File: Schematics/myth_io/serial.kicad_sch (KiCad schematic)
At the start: 7 parts, among them U1 74HC14, U2 74LS02, U5 74AHC04, U6 74HC74, U7 74HC595, U8 74HC165

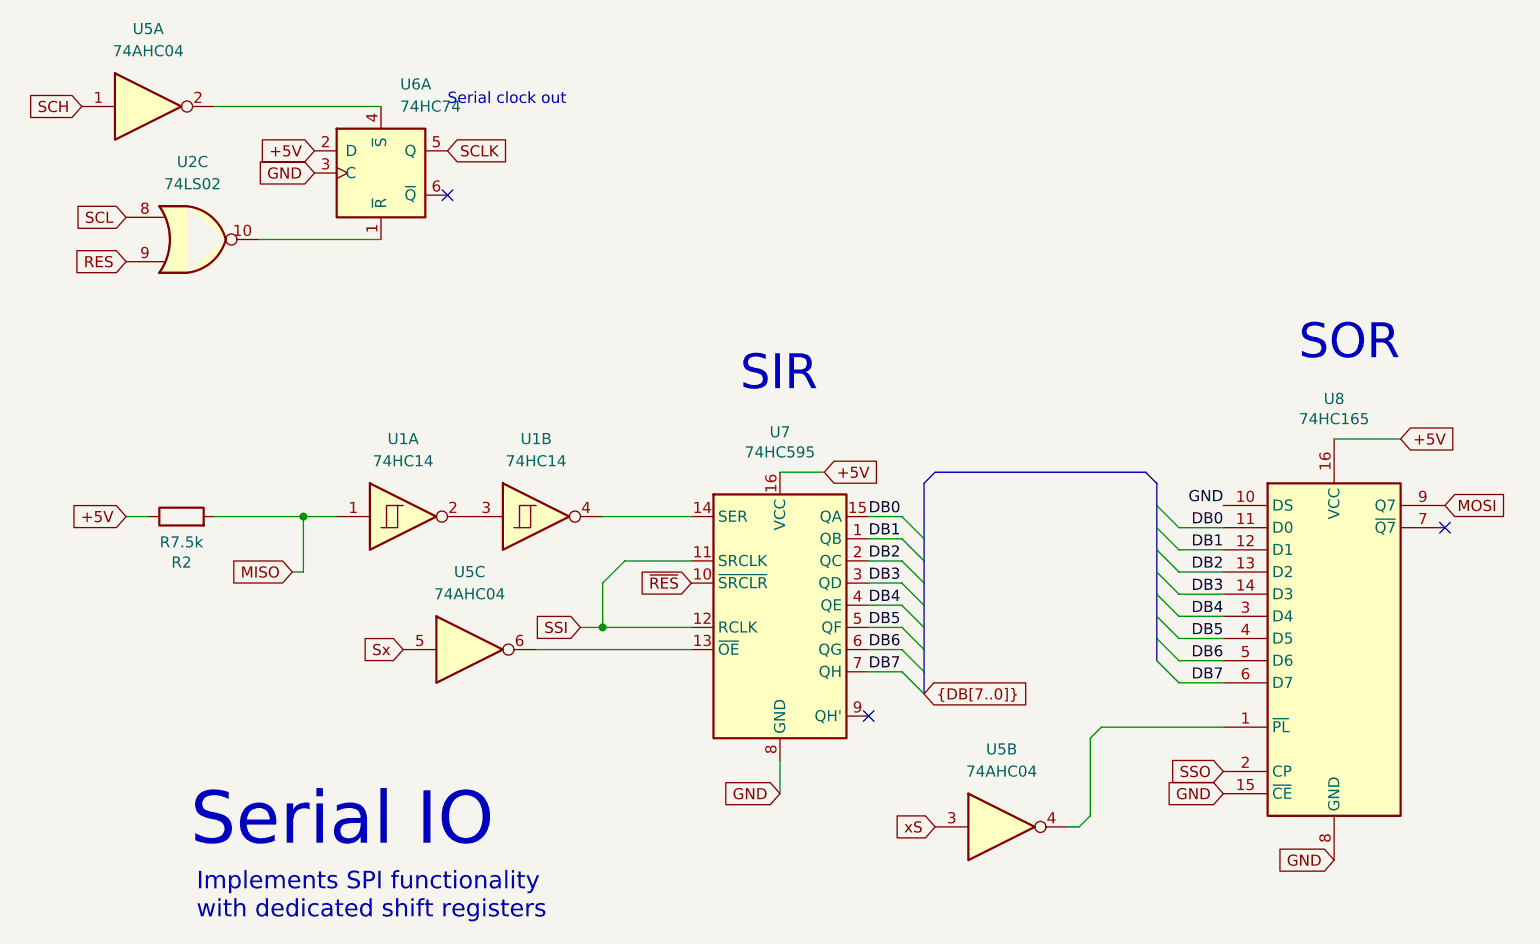
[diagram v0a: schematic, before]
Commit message: Change CO do D
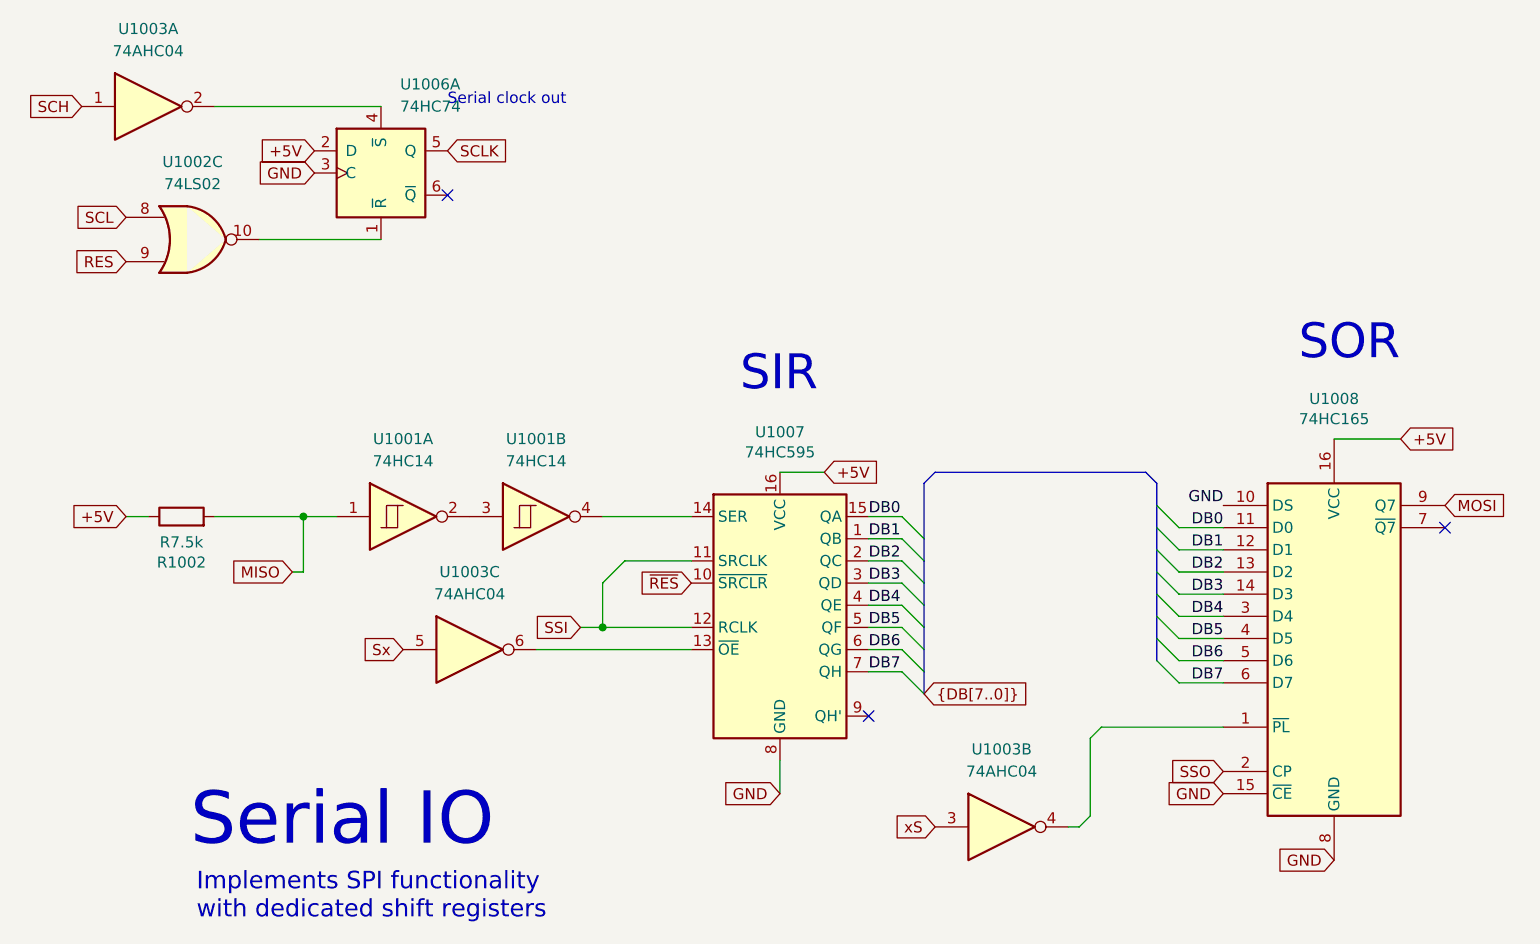
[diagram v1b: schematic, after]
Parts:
- renumbered R2 to R1002, U1 to U1001, U2 to U1002, U5 to U1003, U6 to U1006, U7 to U1007, U8 to U1008
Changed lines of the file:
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@@
 		(dnp no)
 		(fields_autoplaced yes)
-		(property "Reference" "U5"
+		(property "Reference" "U1003"
 			(at 77.47 38.1 0)
 			(effects
@@
 			(project "myth_io"
 				(path "/a907dd88-e0e4-4e6e-a291-053f6213a316/1a18eb1f-a528-4c0e-842f-5264d74e97c6"
-					(reference "U5")
+					(reference "U1003")
 					(unit 1)
 				)
@@
 		(on_board yes)
 		(dnp no)
-		(property "Reference" "U7"
+		(property "Reference" "U1007"
 			(at 149.86 84.3026 0)
 			(effects
@@
 			(project "myth_io"
 				(path "/a907dd88-e0e4-4e6e-a291-053f6213a316/1a18eb1f-a528-4c0e-842f-5264d74e97c6"
-					(reference "U7")
+					(reference "U1007")
 					(unit 1)
 				)
@@
 		(dnp no)
 		(fields_autoplaced yes)
-		(property "Reference" "U5"
+		(property "Reference" "U1003"
 			(at 114.3 100.33 0)
 			(effects
@@
 			(project "myth_io"
 				(path "/a907dd88-e0e4-4e6e-a291-053f6213a316/1a18eb1f-a528-4c0e-842f-5264d74e97c6"
-					(reference "U5")
+					(reference "U1003")
 					(unit 3)
 				)
@@
 		(on_board yes)
 		(dnp no)
-		(property "Reference" "R2"
+		(property "Reference" "R1002"
 			(at 81.28 99.2378 90)
 			(effects
@@
 			(project "myth_io"
 				(path "/a907dd88-e0e4-4e6e-a291-053f6213a316/1a18eb1f-a528-4c0e-842f-5264d74e97c6"
-					(reference "R2")
+					(reference "R1002")
 					(unit 1)
 				)
@@
 		(dnp no)
 		(fields_autoplaced yes)
-		(property "Reference" "U1"
+		(property "Reference" "U1001"
 			(at 106.68 85.09 0)
 			(effects
@@
 			(project "myth_io"
 				(path "/a907dd88-e0e4-4e6e-a291-053f6213a316/1a18eb1f-a528-4c0e-842f-5264d74e97c6"
-					(reference "U1")
+					(reference "U1001")
 					(unit 1)
 				)
@@
 		(on_board yes)
 		(dnp no)
-		(property "Reference" "U8"
+		(property "Reference" "U1008"
 			(at 213.36 80.4926 0)
 			(effects
@@
 			(project "myth_io"
 				(path "/a907dd88-e0e4-4e6e-a291-053f6213a316/1a18eb1f-a528-4c0e-842f-5264d74e97c6"
-					(reference "U8")
+					(reference "U1008")
 					(unit 1)
 				)
@@
 		(dnp no)
 		(fields_autoplaced yes)
-		(property "Reference" "U2"
+		(property "Reference" "U1002"
 			(at 82.55 53.34 0)
 			(effects
@@
 			(project "myth_io"
 				(path "/a907dd88-e0e4-4e6e-a291-053f6213a316/1a18eb1f-a528-4c0e-842f-5264d74e97c6"
-					(reference "U2")
+					(reference "U1002")
 					(unit 3)
 				)
@@
 		(dnp no)
 		(fields_autoplaced yes)
-		(property "Reference" "U1"
+		(property "Reference" "U1001"
 			(at 121.92 85.09 0)
 			(effects
@@
 			(project "myth_io"
 				(path "/a907dd88-e0e4-4e6e-a291-053f6213a316/1a18eb1f-a528-4c0e-842f-5264d74e97c6"
-					(reference "U1")
+					(reference "U1001")
 					(unit 2)
 				)
@@
 		(dnp no)
 		(fields_autoplaced yes)
-		(property "Reference" "U6"
+		(property "Reference" "U1006"
 			(at 106.3341 44.45 0)
 			(effects
@@
 			(project ""
 				(path "/a907dd88-e0e4-4e6e-a291-053f6213a316/1a18eb1f-a528-4c0e-842f-5264d74e97c6"
-					(reference "U6")
+					(reference "U1006")
 					(unit 1)
 				)
@@
 		(on_board yes)
 		(dnp no)
-		(property "Reference" "U5"
+		(property "Reference" "U1003"
 			(at 175.26 120.65 0)
 			(effects
@@
 			(project "myth_io"
 				(path "/a907dd88-e0e4-4e6e-a291-053f6213a316/1a18eb1f-a528-4c0e-842f-5264d74e97c6"
-					(reference "U5")
+					(reference "U1003")
 					(unit 2)
 				)
